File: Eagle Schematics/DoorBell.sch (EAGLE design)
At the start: 9 parts, among them T1 2N3906

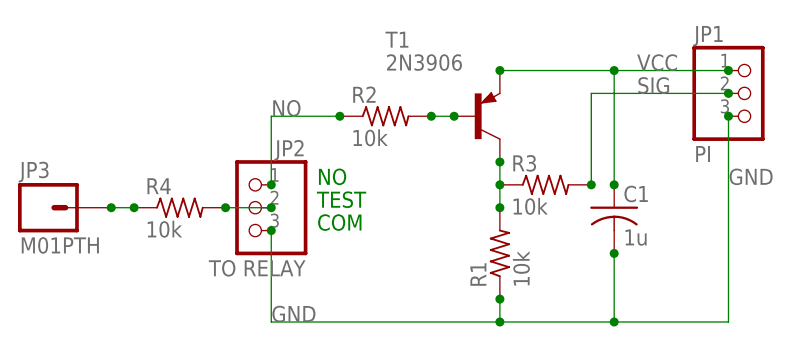
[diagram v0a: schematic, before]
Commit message: Improved Board Labels
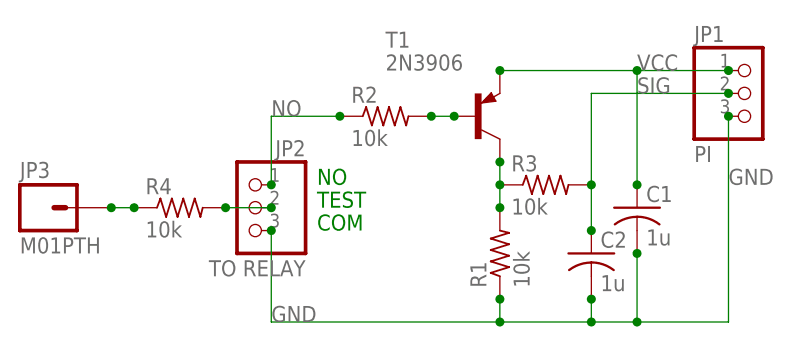
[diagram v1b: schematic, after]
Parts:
- added C2: 1u, rcl:C-US025-025X050
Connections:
- net GND: now also C2.2
- net SIG: now also C2.1
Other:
- moved on the sheet: C1
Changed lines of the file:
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@@
 <part name="JP3" library="SparkFun-Connectors" deviceset="M01" device="PTH"/>
 <part name="R4" library="resistor" deviceset="R-US_" device="0204/5" value="10k"/>
+<part name="C2" library="rcl" deviceset="C-US" device="025-025X050" value="1u"/>
 </parts>
 <sheets>
@@
 <instance part="R3" gate="G$1" x="66.04" y="45.72"/>
 <instance part="JP2" gate="A" x="33.02" y="43.18" rot="MR0"/>
-<instance part="C1" gate="G$1" x="73.66" y="43.18"/>
+<instance part="C1" gate="G$1" x="76.2" y="43.18"/>
 <instance part="T1" gate="G$1" x="58.42" y="53.34"/>
 <instance part="R1" gate="G$1" x="60.96" y="38.1" rot="R90"/>
@@
 <instance part="JP3" gate="G$1" x="10.16" y="43.18"/>
 <instance part="R4" gate="G$1" x="25.4" y="43.18"/>
+<instance part="C2" gate="G$1" x="71.12" y="38.1"/>
 </instances>
 <busses>
@@
 <pinref part="JP1" gate="A" pin="1"/>
 <junction x="86.36" y="58.42"/>
-<junction x="73.66" y="58.42"/>
-<wire x1="73.66" y1="58.42" x2="86.36" y2="58.42" width="0.1524" layer="91"/>
+<junction x="76.2" y="58.42"/>
+<wire x1="76.2" y1="58.42" x2="86.36" y2="58.42" width="0.1524" layer="91"/>
 <pinref part="C1" gate="G$1" pin="1"/>
-<junction x="73.66" y="45.72"/>
-<wire x1="73.66" y1="58.42" x2="73.66" y2="45.72" width="0.1524" layer="91"/>
+<junction x="76.2" y="45.72"/>
+<wire x1="76.2" y1="58.42" x2="76.2" y2="45.72" width="0.1524" layer="91"/>
 <pinref part="T1" gate="G$1" pin="E"/>
 <junction x="60.96" y="58.42"/>
-<wire x1="60.96" y1="58.42" x2="73.66" y2="58.42" width="0.1524" layer="91"/>
+<wire x1="60.96" y1="58.42" x2="76.2" y2="58.42" width="0.1524" layer="91"/>
 <label x="76.2" y="58.42" size="1.778" layer="95"/>
 </segment>
@@
 <pinref part="JP1" gate="A" pin="3"/>
 <junction x="86.36" y="53.34"/>
-<wire x1="60.96" y1="30.48" x2="73.66" y2="30.48" width="0.1524" layer="91"/>
-<wire x1="73.66" y1="30.48" x2="86.36" y2="30.48" width="0.1524" layer="91"/>
+<wire x1="60.96" y1="30.48" x2="71.12" y2="30.48" width="0.1524" layer="91"/>
+<wire x1="71.12" y1="30.48" x2="76.2" y2="30.48" width="0.1524" layer="91"/>
+<wire x1="76.2" y1="30.48" x2="86.36" y2="30.48" width="0.1524" layer="91"/>
 <wire x1="86.36" y1="30.48" x2="86.36" y2="53.34" width="0.1524" layer="91"/>
-<junction x="73.66" y="30.48"/>
+<junction x="76.2" y="30.48"/>
 <pinref part="C1" gate="G$1" pin="2"/>
-<junction x="73.66" y="38.1"/>
-<wire x1="73.66" y1="38.1" x2="73.66" y2="30.48" width="0.1524" layer="91"/>
+<junction x="76.2" y="38.1"/>
+<wire x1="76.2" y1="38.1" x2="76.2" y2="30.48" width="0.1524" layer="91"/>
 <junction x="60.96" y="30.48"/>
 <pinref part="R1" gate="G$1" pin="1"/>
@@
 <label x="35.56" y="30.48" size="1.778" layer="95"/>
 <label x="86.36" y="45.72" size="1.778" layer="95"/>
+<junction x="71.12" y="30.48"/>
+<pinref part="C2" gate="G$1" pin="2"/>
+<junction x="71.12" y="33.02"/>
+<wire x1="71.12" y1="33.02" x2="71.12" y2="30.48" width="0.1524" layer="91"/>
 </segment>
 </net>
@@
 <wire x1="71.12" y1="55.88" x2="86.36" y2="55.88" width="0.1524" layer="91"/>
 <label x="76.2" y="55.88" size="1.778" layer="95"/>
+<pinref part="C2" gate="G$1" pin="1"/>
+<junction x="71.12" y="40.64"/>
+<wire x1="71.12" y1="40.64" x2="71.12" y2="45.72" width="0.1524" layer="91"/>
 </segment>
 </net>
